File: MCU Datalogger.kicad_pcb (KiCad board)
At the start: 4 copper layers, 51.4 x 34.3 mm, 31 parts, among them J1 Conn_01x04_Male, J2 Conn_01x09_Male, J3 Conn_01x04_Male, J4 Conn_02x03_Odd_Even, U1 24LC1025, U2 DS1337S+, U3 24LC1025, U4 ATMEGA328P-AU, Y1 32.768 KHz, Y2 16 MHz

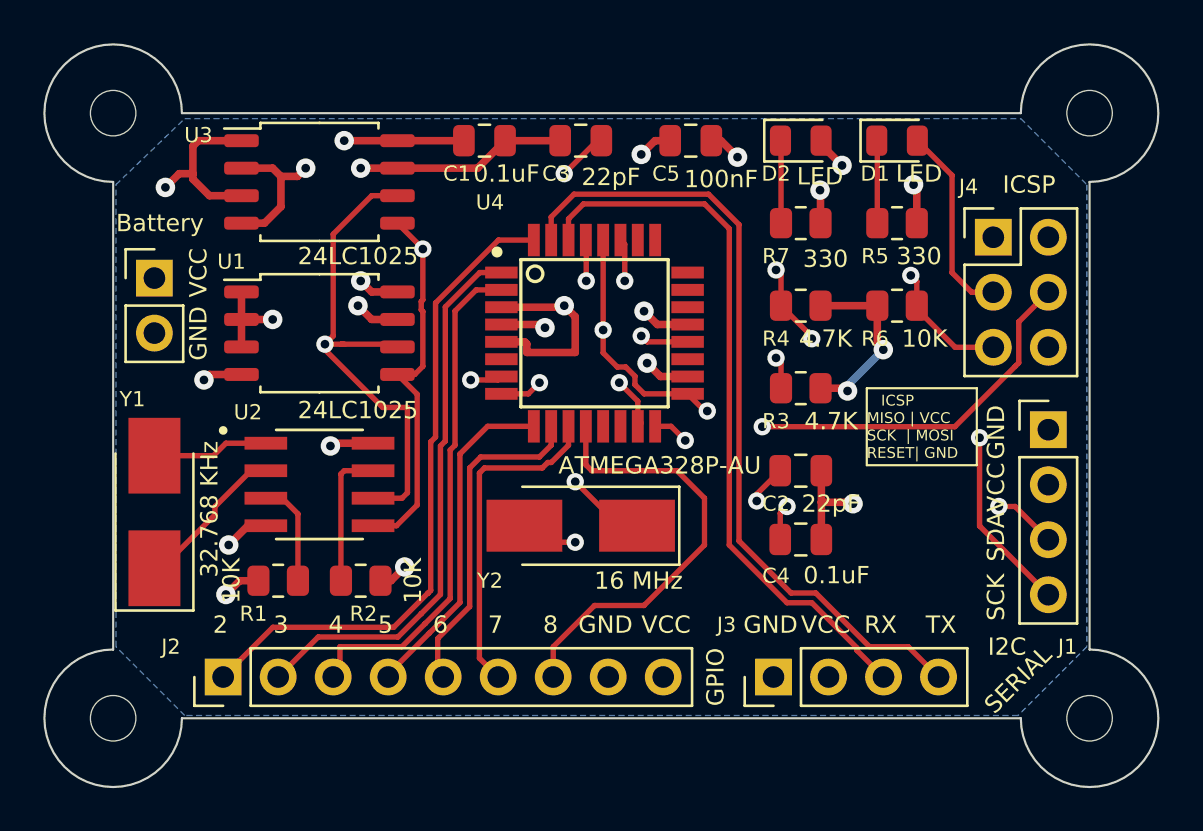
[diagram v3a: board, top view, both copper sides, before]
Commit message: Fixed errata #106
I2C clock should be named SCL and not connected to SPI click net SCK
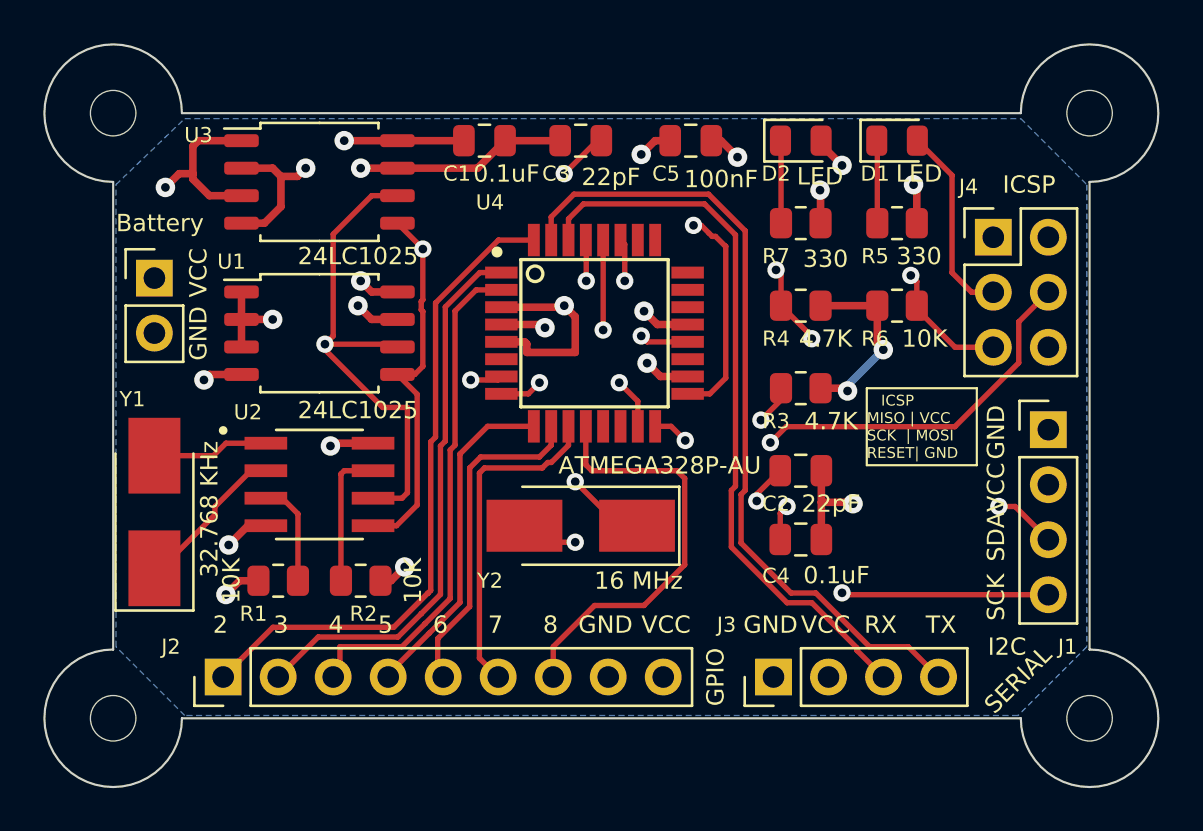
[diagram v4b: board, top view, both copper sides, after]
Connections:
- net /Abc123 renamed Net-(C4-Pad2)
- J1 pad 4: /SCK -> /SCL
- R3 pad 2: /SCK -> /SCL
- U1 pad 6: /SCK -> /SCL
- U2 pad 6: /SCK -> /SCL
- U3 pad 6: /SCK -> /SCL
- U4 pad 13: (no net) -> unconnected-(U4-Pad13)
- U4 pad 14: (no net) -> unconnected-(U4-Pad14)
- U4 pad 19: (no net) -> unconnected-(U4-Pad19)
- U4 pad 22: (no net) -> unconnected-(U4-Pad22)
- U4 pad 23: (no net) -> unconnected-(U4-Pad23)
- U4 pad 24: (no net) -> unconnected-(U4-Pad24)
- U4 pad 25: (no net) -> unconnected-(U4-Pad25)
- U4 pad 26: (no net) -> unconnected-(U4-Pad26)
- U4 pad 28: /SCK -> /SCL
- U4 pad 6: (no net) -> unconnected-(U4-Pad6)
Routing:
- net /SCL: track 0.00 -> 74.2 mm, vias 0 -> 4
- net /SCK: track 90.8 -> 34.2 mm, vias 5 -> 1
- net /D8: track 20.4 -> 19.6 mm
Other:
- outline, holes or cut-outs redrawn
- board text removed: "- 2Mbit EEPROM - RTC - I2C, SPI, GPIOs"
